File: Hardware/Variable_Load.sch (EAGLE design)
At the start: 52 parts, among them Q1 60V/32A/35mΩ, U1 CY8C5868LTI-LP039, U2 3.3V

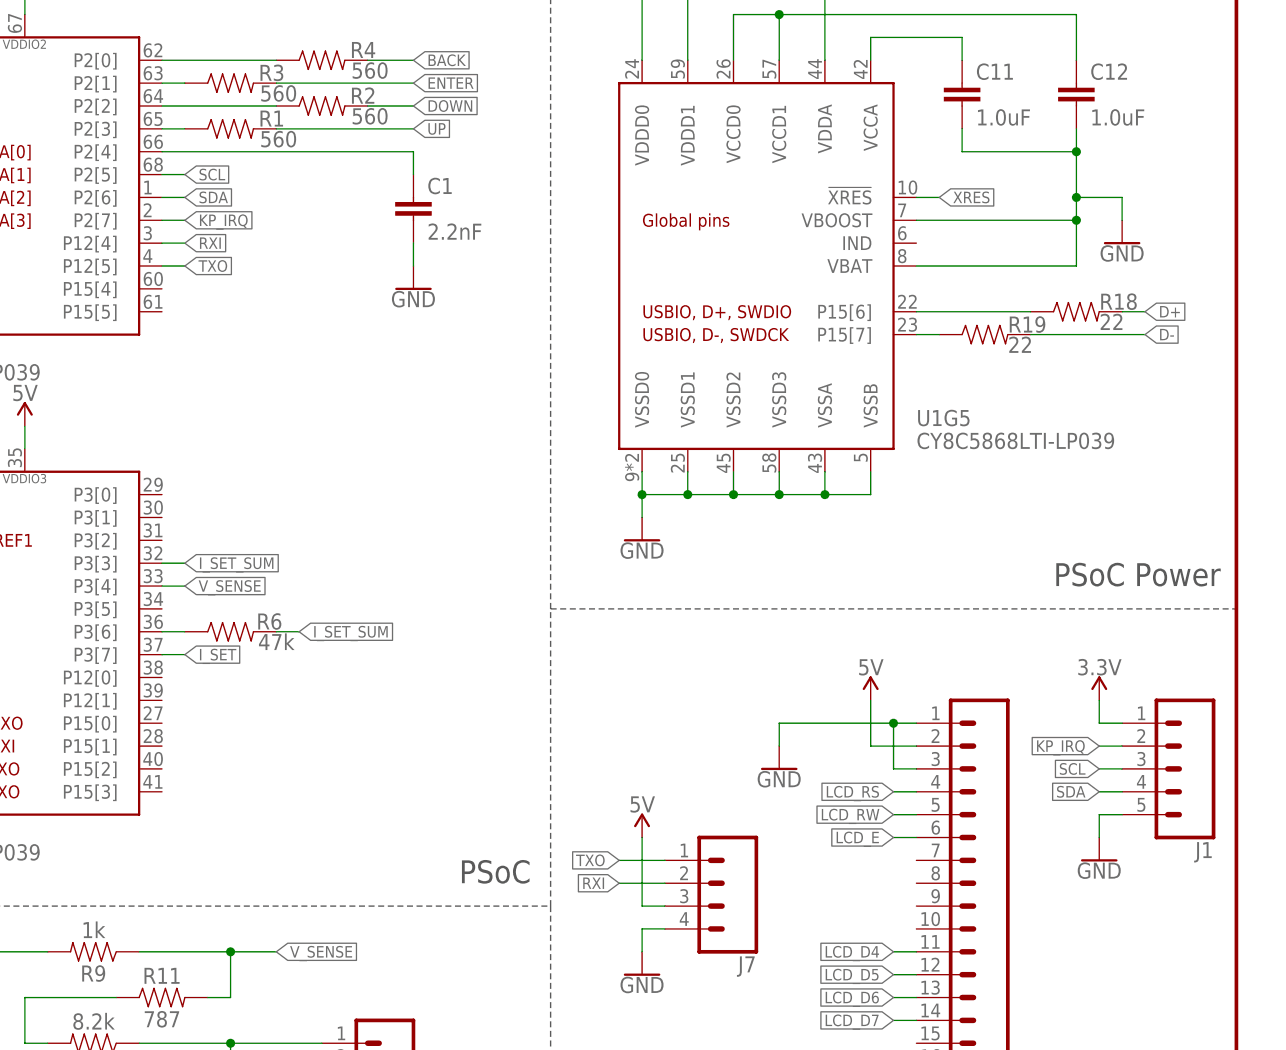
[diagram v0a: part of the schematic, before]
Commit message: Removed header for CT keypad
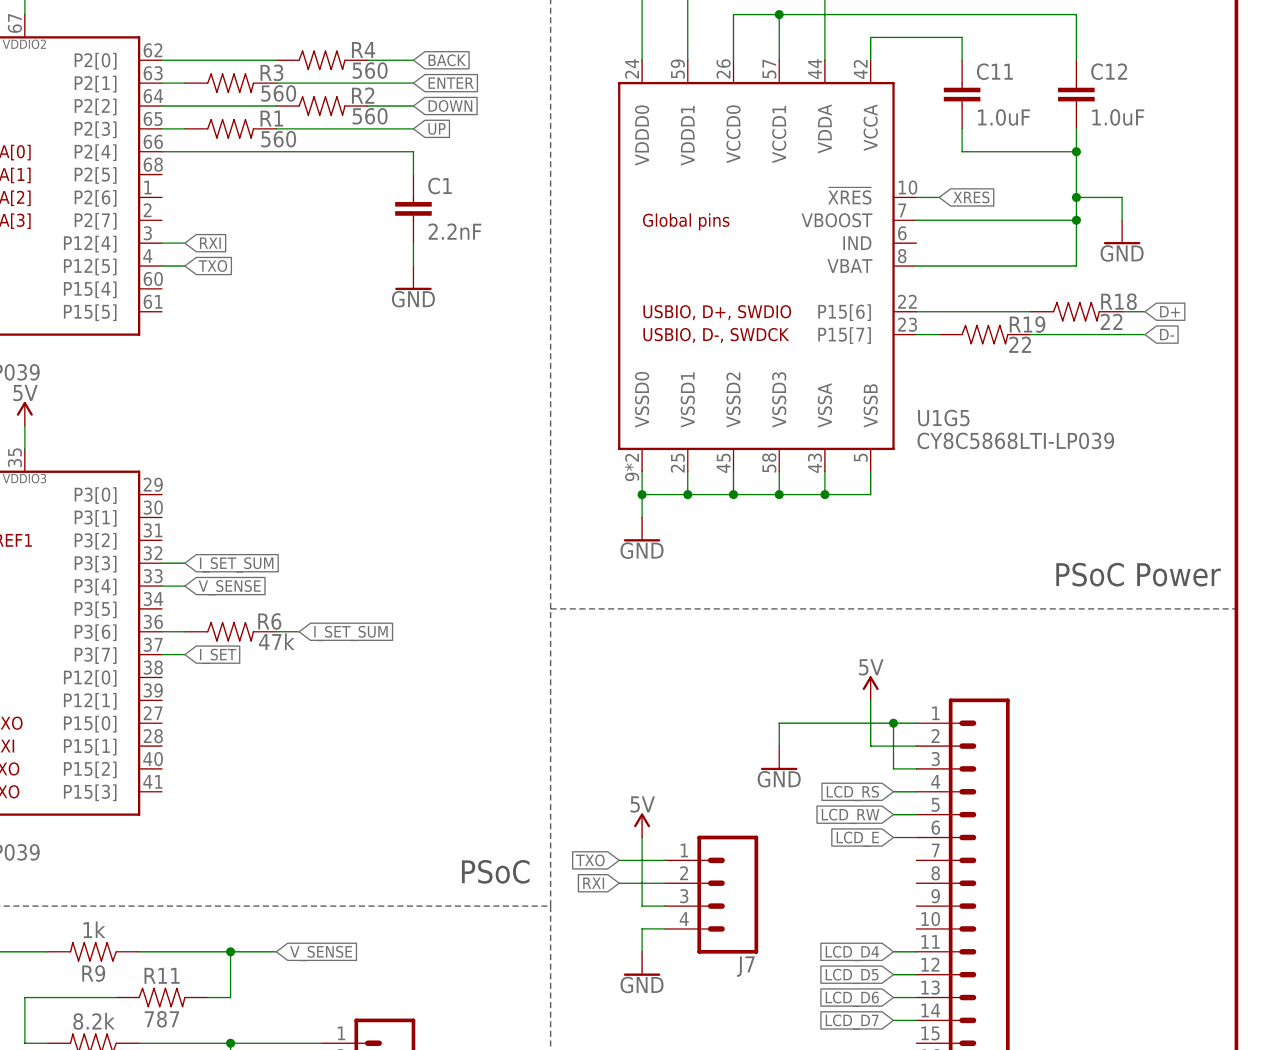
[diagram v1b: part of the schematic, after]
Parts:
- removed J1: (no value), SparkFun-Connectors:CONN_05
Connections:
- removed net KP_IRQ: J1.2, U1G3.P2[7]
- removed net SCL: J1.3, U1G3.P2[5]
- removed net SDA: J1.4, U1G3.P2[6]
- net 3.3V: no longer J1.1
- net GND: no longer J1.5
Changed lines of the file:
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@@
 <part name="R19" library="SparkFun-Resistors" deviceset="22OHM1/10W1%(0402)" device="" value="22"/>
 <part name="GND3" library="SparkFun-PowerSymbols" deviceset="GND" device=""/>
-<part name="J1" library="SparkFun-Connectors" deviceset="CONN_05" device=""/>
 <part name="J2" library="SparkFun-Connectors" deviceset="CONN_16" device=""/>
-<part name="GND5" library="SparkFun-PowerSymbols" deviceset="GND" device=""/>
-<part name="SUPPLY9" library="SparkFun-PowerSymbols" deviceset="3.3V" device=""/>
 <part name="GND6" library="SparkFun-PowerSymbols" deviceset="GND" device=""/>
 <part name="SUPPLY10" library="SparkFun-PowerSymbols" deviceset="5V" device=""/>
@@
 </instance>
 <instance part="GND3" gate="1" x="182.88" y="116.84"/>
-<instance part="J1" gate="G$1" x="243.84" y="91.44" rot="R180"/>
 <instance part="J2" gate="G$1" x="223.52" y="76.2" rot="R180"/>
-<instance part="GND5" gate="1" x="233.68" y="81.28"/>
-<instance part="SUPPLY9" gate="G$1" x="233.68" y="99.06"/>
 <instance part="GND6" gate="1" x="198.12" y="91.44"/>
 <instance part="SUPPLY10" gate="G$1" x="208.28" y="99.06"/>
@@
 </segment>
 <segment>
-<pinref part="GND5" gate="1" pin="GND"/>
-<wire x1="233.68" y1="83.82" x2="233.68" y2="86.36" width="0.1524" layer="91"/>
-<pinref part="J1" gate="G$1" pin="5"/>
-<wire x1="233.68" y1="86.36" x2="236.22" y2="86.36" width="0.1524" layer="91"/>
-</segment>
-<segment>
 <pinref part="GND6" gate="1" pin="GND"/>
 <wire x1="198.12" y1="93.98" x2="198.12" y2="96.52" width="0.1524" layer="91"/>
@@
 <pinref part="U1" gate="G3" pin="VDDIO2"/>
 <wire x1="114.3" y1="177.8" x2="114.3" y2="175.26" width="0.1524" layer="91"/>
-</segment>
-<segment>
-<pinref part="SUPPLY9" gate="G$1" pin="3.3V"/>
-<wire x1="233.68" y1="99.06" x2="233.68" y2="96.52" width="0.1524" layer="91"/>
-<pinref part="J1" gate="G$1" pin="1"/>
-<wire x1="233.68" y1="96.52" x2="236.22" y2="96.52" width="0.1524" layer="91"/>
 </segment>
 <segment>
@@
 </segment>
 </net>
-<net name="SCL" class="0">
-<segment>
-<pinref part="U1" gate="G3" pin="P2[5]"/>
-<wire x1="129.54" y1="157.48" x2="132.08" y2="157.48" width="0.1524" layer="91"/>
-<label x="132.08" y="157.48" size="1.27" layer="95" xref="yes"/>
-</segment>
-<segment>
-<pinref part="J1" gate="G$1" pin="3"/>
-<wire x1="236.22" y1="91.44" x2="233.68" y2="91.44" width="0.1524" layer="91"/>
-<label x="233.68" y="91.44" size="1.27" layer="95" rot="R180" xref="yes"/>
-</segment>
-</net>
-<net name="SDA" class="0">
-<segment>
-<pinref part="U1" gate="G3" pin="P2[6]"/>
-<wire x1="129.54" y1="154.94" x2="132.08" y2="154.94" width="0.1524" layer="91"/>
-<label x="132.08" y="154.94" size="1.27" layer="95" xref="yes"/>
-</segment>
-<segment>
-<pinref part="J1" gate="G$1" pin="4"/>
-<wire x1="236.22" y1="88.9" x2="233.68" y2="88.9" width="0.1524" layer="91"/>
-<label x="233.68" y="88.9" size="1.27" layer="95" rot="R180" xref="yes"/>
-</segment>
-</net>
-<net name="KP_IRQ" class="0">
-<segment>
-<pinref part="U1" gate="G3" pin="P2[7]"/>
-<wire x1="129.54" y1="152.4" x2="132.08" y2="152.4" width="0.1524" layer="91"/>
-<label x="132.08" y="152.4" size="1.27" layer="95" xref="yes"/>
-</segment>
-<segment>
-<pinref part="J1" gate="G$1" pin="2"/>
-<wire x1="233.68" y1="93.98" x2="236.22" y2="93.98" width="0.1524" layer="91"/>
-<label x="233.68" y="93.98" size="1.27" layer="95" rot="R180" xref="yes"/>
-</segment>
-</net>
